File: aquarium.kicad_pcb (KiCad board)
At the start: 2 copper layers, 108.5 x 99.5 mm, 16 parts, among them J1 DC Input, J2 LED 1 Output, J3 LED 2 Output, Q1 IRLZ44N, SW1 Interval reset, SW2 Power switch, U1 DS3231, U2 TC4426ACPA

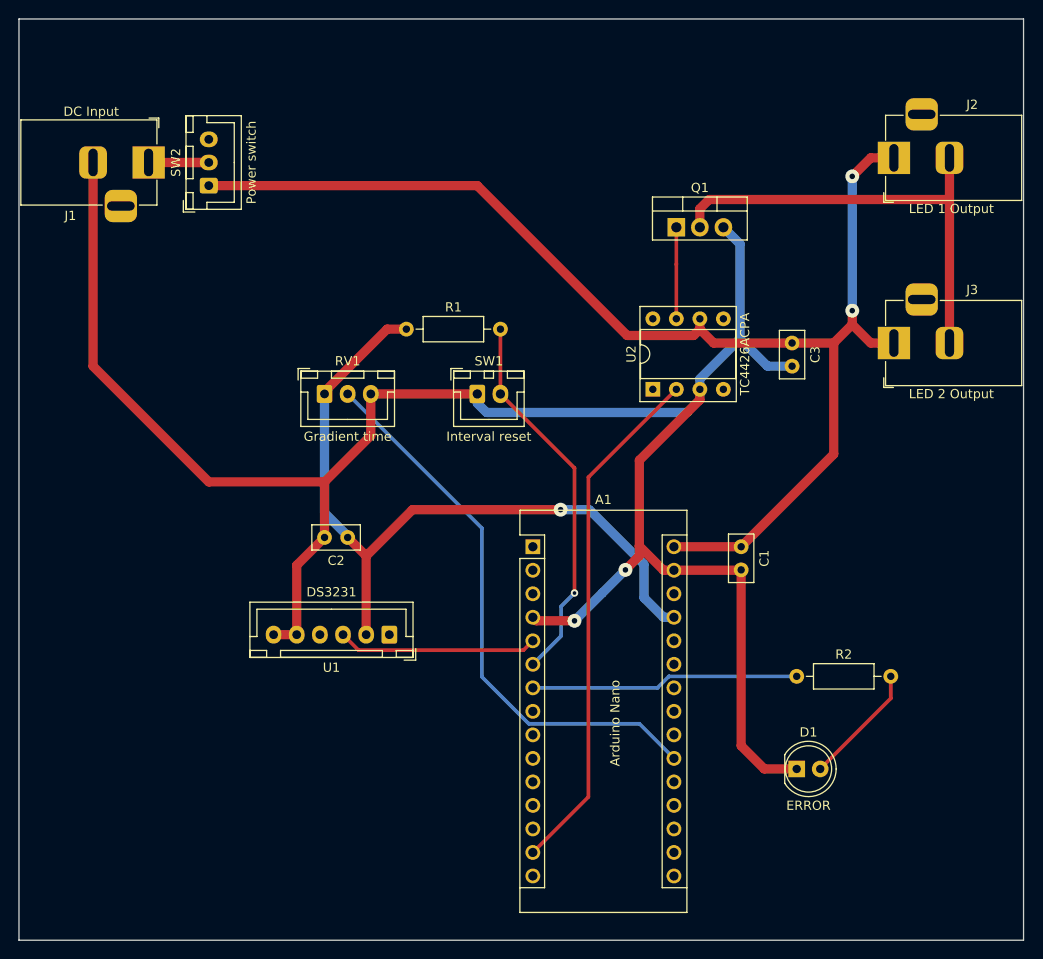
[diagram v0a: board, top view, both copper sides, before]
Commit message: update the pcb design with the new footprints
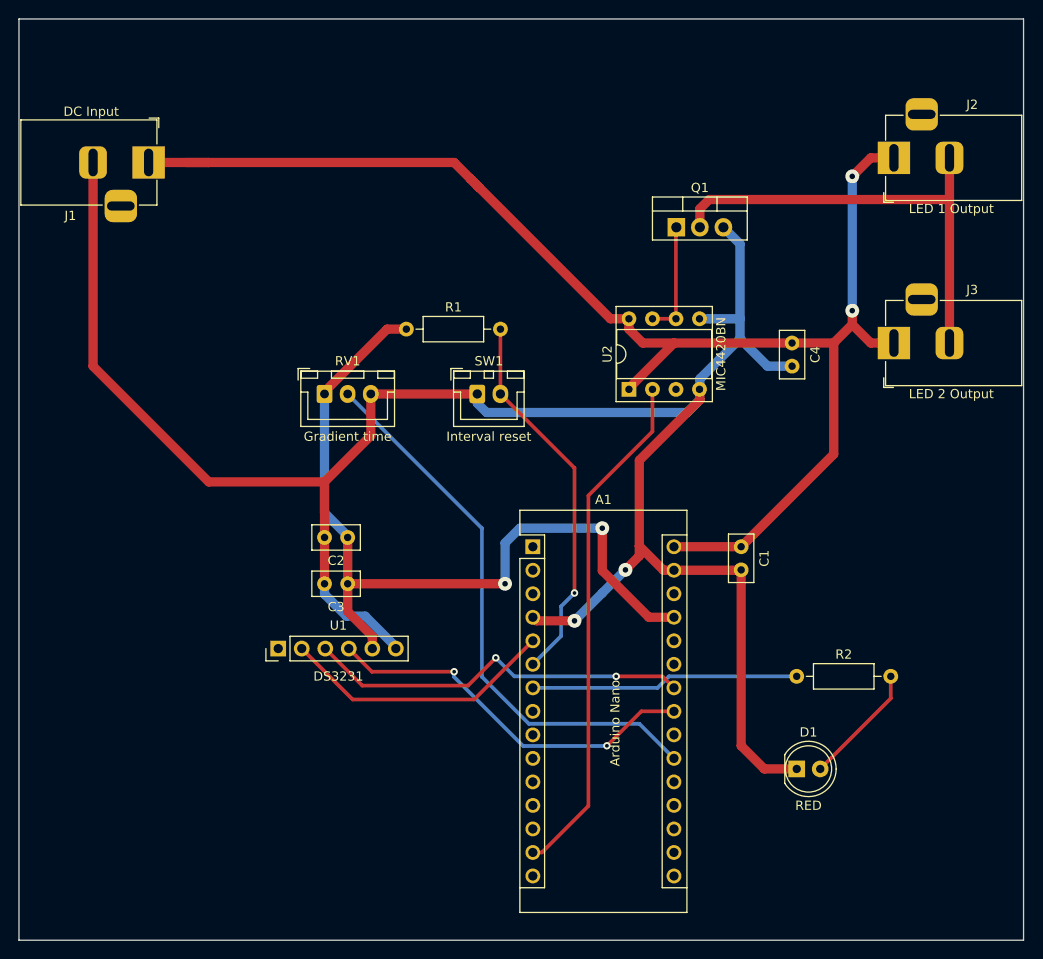
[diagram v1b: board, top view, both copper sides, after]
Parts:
- removed SW2: Power switch, Connector_JST:JST_XH_B3B-XH-A_1x03_P2.50mm_Vertical
- added C3: 0.1u, Capacitor_THT:C_Disc_D5.0mm_W2.5mm_P2.50mm, F.Cu at (100.5, 117.0)
- C1: value 1u-100u -> 10u
- C2: value 0.1u-1u -> 0.1u
- C4: renamed from C3; value 1u-100u -> 10u
- D1: value ERROR -> RED
- U1: footprint Connector_JST:JST_XH_B6B-XH-A_1x06_P2.50mm_Vertical -> Connector_PinHeader_2.54mm:PinHeader_1x06_P2.54mm_Vertical
- U2: value TC4426ACPA -> MIC4420BN
- moved U1 12.1 mm to (93.0, 124.0), turned to 90 degrees
- moved U2 2.58 mm to (130.9, 96.0)
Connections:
- A1 pad 23: (no net) -> SDA
- A1 pad 24: (no net) -> SCL
- J1 pad 1: VCC_CON -> +12V
- Q1 pad 1: Net-(Q1-Pad1) -> /MOSFET_OUT
- U1 pad 2: +5V -> INT
- U1 pad 3: INT -> SCL
- U1 pad 4: (no net) -> SDA
- U1 pad 5: GND -> +5V
- U2 pad 1: (no net) -> +12V
- U2 pad 3: GND -> (no net)
- U2 pad 4: (no net) -> GND
- U2 pad 5: (no net) -> GND
- U2 pad 6: +12V -> /MOSFET_OUT
- U2 pad 7: Net-(Q1-Pad1) -> /MOSFET_OUT
- U2 pad 8: (no net) -> +12V
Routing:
- net SCL: track 0.00 -> 41.9 mm, vias 0 -> 2
- net SDA: track 0.00 -> 41.4 mm, vias 0 -> 2
- net +12V: track 139.1 -> 156.9 mm
- net /MOSFET_OUT: track 0.00 -> 12.4 mm
- net Net-(Q1-Pad1): track 9.88 -> 0.00 mm
- net VCC_CON: track 9.00 -> 0.00 mm
- net INT: track 21.6 -> 29.9 mm
- net +5V: track 82.0 -> 88.5 mm, vias 1 -> 2
- net GND: track 222.9 -> 229.5 mm
